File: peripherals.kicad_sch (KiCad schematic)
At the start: 14 parts, among them U5 FT230XQ

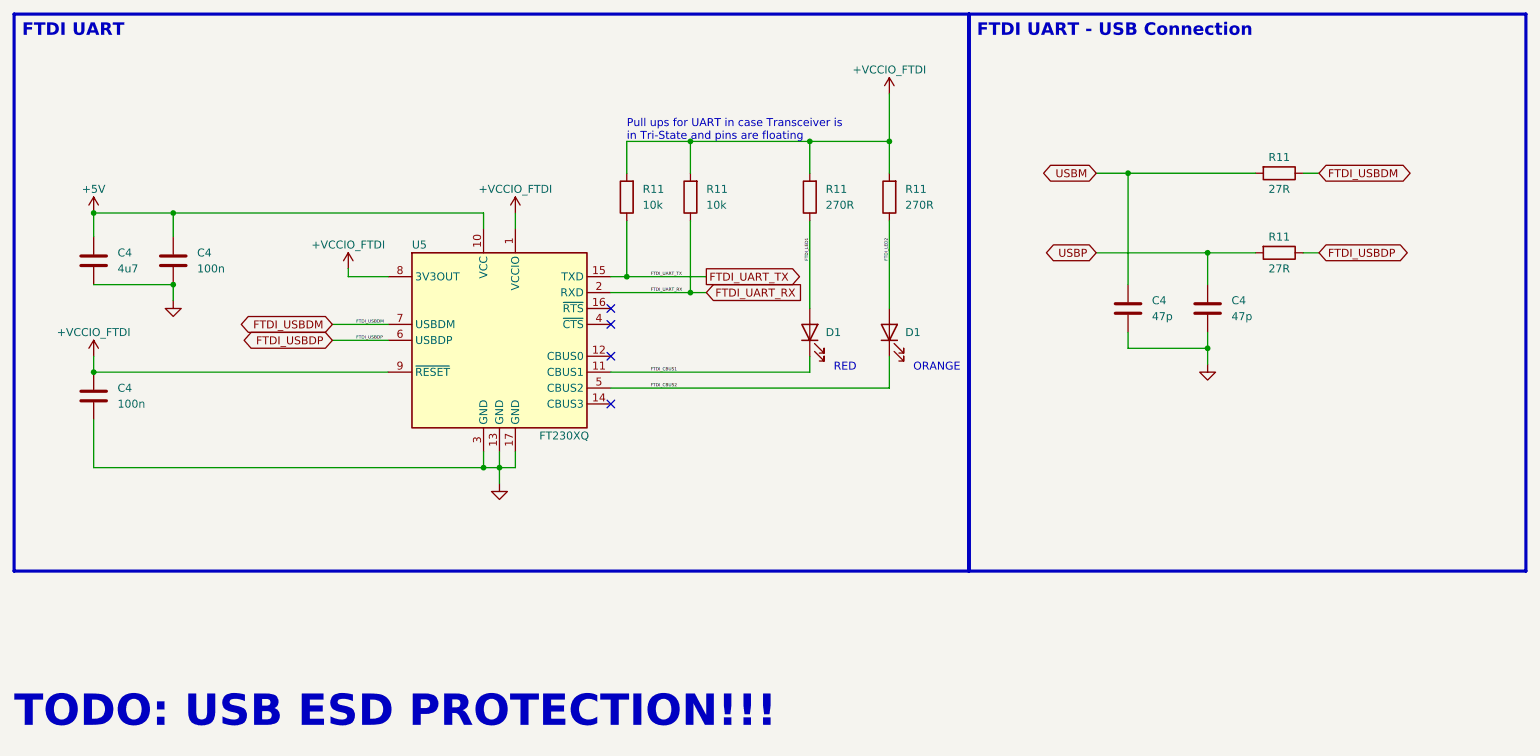
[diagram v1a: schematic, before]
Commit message: Schematic is done for now, starting layout
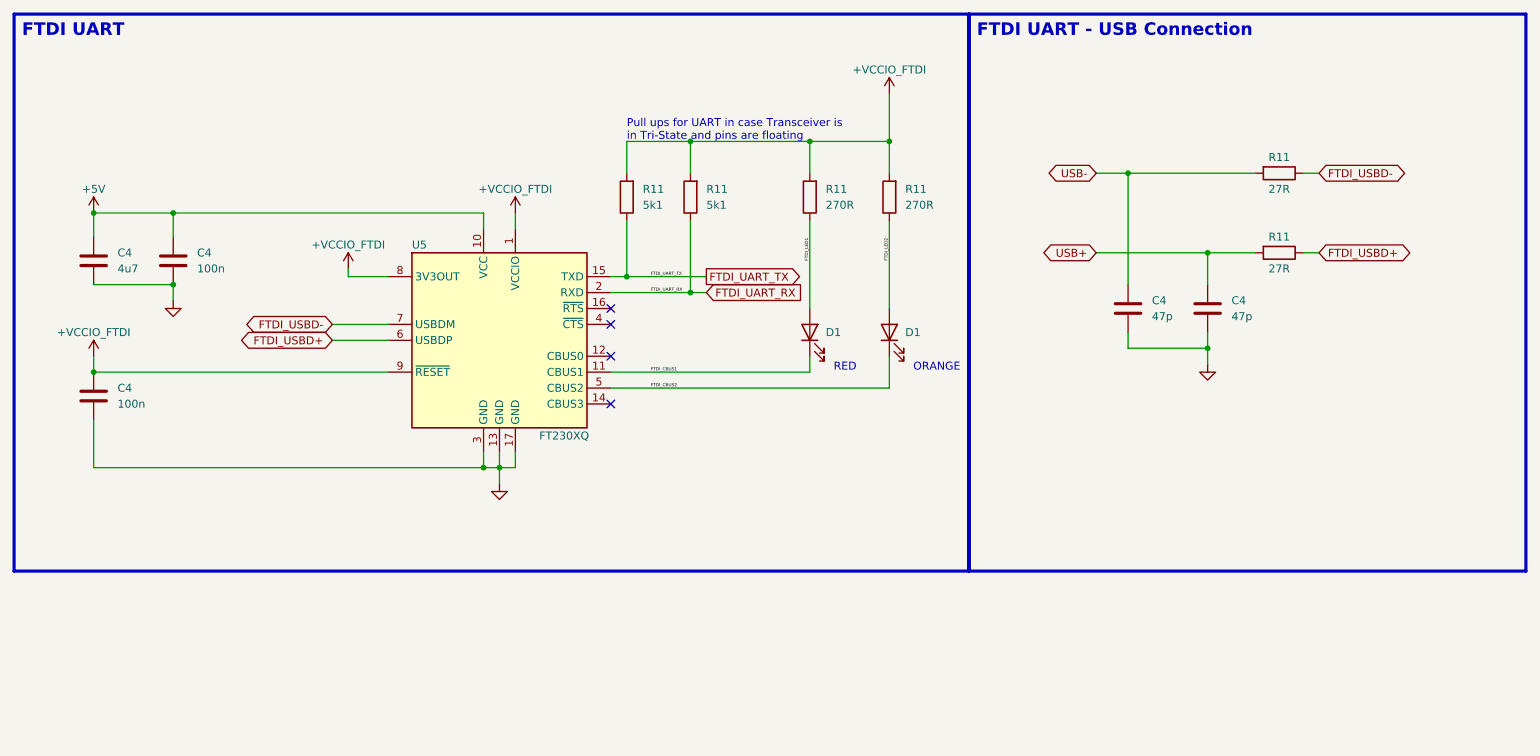
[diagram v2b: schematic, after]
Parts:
- D1: Distributor Link (none) -> https://www.mouser.de/ProductDetail/Lumex/SML-LX0402SIC-TR?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; MFN SML-LX0402SIC-TR -> (none); Manufacturer (none) -> Lumex; Manufacturer Number (none) -> SML-LX0402SIC-TR
- D1: Distributor Link (none) -> https://www.mouser.de/ProductDetail/Lumex/SML-LX0402SOC-TR?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; MFN SML-LX0402SOC-TR -> (none); Manufacturer (none) -> Lumex; Manufacturer Number (none) -> SML-LX0402SOC-TR
- R11: value 10k -> 5k1
- U5: Distributor Link (none) -> https://www.mouser.de/ProductDetail/FTDI/FT230XQ-R?qs=Gp1Yz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; Manufacturer (none) -> FTDI; Manufacturer Number (none) -> FT230XQ-R
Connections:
- net FTDI_USBDM renamed FTDI_USBD-
- net FTDI_USBDP renamed FTDI_USBD+
- net USBM renamed USB-
- net USBP renamed USB+
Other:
- note removed: "TODO: USB ESD PROTECTION!!!"
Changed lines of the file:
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@@
     (effects (font (size 2 2) (thickness 0.254) bold (color 100 100 100 1)) (justify left bottom))
-  )
-  (text "TODO: USB ESD PROTECTION!!!" (at 25.4 139.7 0)
-    (effects (font (size 5 5) (thickness 1) bold (color 150 0 0 1)) (justify left bottom))
   )
   (text "Pull ups for UART in case Transceiver is\nin Tri-State and pins are floating"
@@
     )
   )
-  (label "FTDI_USBDP" (at 80.01 77.47 0) (fields_autoplaced)
-    (effects (font (size 0.5 0.5)) (justify left bottom))
-    (property "Netclass" "UART" (at 80.01 77.97 0)
-      (effects (font (size 0.5 0.5) italic) (justify left))
-    )
-  )
   (label "FTDI_LED1" (at 152.4 64.77 90) (fields_autoplaced)
     (effects (font (size 0.5 0.5)) (justify left bottom))
@@
     )
   )
-  (label "FTDI_USBDM" (at 80.01 74.93 0) (fields_autoplaced)
-    (effects (font (size 0.5 0.5)) (justify left bottom))
-    (property "Netclass" "UART" (at 80.01 75.43 0)
-      (effects (font (size 0.5 0.5) italic) (justify left))
-    )
-  )
   (label "FTDI_LED2" (at 165.1 64.77 90) (fields_autoplaced)
     (effects (font (size 0.5 0.5)) (justify left bottom))
@@
     )
   )
-  (global_label "FTDI_USBDP" (shape bidirectional) (at 76.2 77.47 180) (fields_autoplaced)
+  (global_label "FTDI_USBD+" (shape bidirectional) (at 76.2 77.47 180) (fields_autoplaced)
     (effects (font (size 1.27 1.27)) (justify right))
-    (property "Intersheetrefs" "${INTERSHEET_REFS}" (at 60.8549 77.47 0)
+    (property "Intersheetrefs" "${INTERSHEET_REFS}" (at 60.5525 77.47 0)
       (effects (font (size 1.27 1.27)) (justify right) hide)
     )
   )
-  (global_label "USBP" (shape bidirectional) (at 198.12 63.5 180) (fields_autoplaced)
+  (global_label "USB+" (shape bidirectional) (at 198.12 63.5 180) (fields_autoplaced)
     (effects (font (size 1.27 1.27)) (justify right))
-    (property "Intersheetrefs" "${INTERSHEET_REFS}" (at 188.9435 63.5 0)
+    (property "Intersheetrefs" "${INTERSHEET_REFS}" (at 188.6411 63.5 0)
       (effects (font (size 1.27 1.27)) (justify right) hide)
     )
   )
-  (global_label "FTDI_USBDM" (shape bidirectional) (at 76.2 74.93 180) (fields_autoplaced)
+  (global_label "FTDI_USBD-" (shape bidirectional) (at 76.2 74.93 180) (fields_autoplaced)
     (effects (font (size 1.27 1.27)) (justify right))
-    (property "Intersheetrefs" "${INTERSHEET_REFS}" (at 60.6735 74.93 0)
+    (property "Intersheetrefs" "${INTERSHEET_REFS}" (at 60.5525 74.93 0)
       (effects (font (size 1.27 1.27)) (justify right) hide)
     )
   )
-  (global_label "FTDI_USBDM" (shape bidirectional) (at 233.68 50.8 0) (fields_autoplaced)
+  (global_label "FTDI_USBD-" (shape bidirectional) (at 233.68 50.8 0) (fields_autoplaced)
     (effects (font (size 1.27 1.27)) (justify left))
-    (property "Intersheetrefs" "${INTERSHEET_REFS}" (at 249.2065 50.8 0)
+    (property "Intersheetrefs" "${INTERSHEET_REFS}" (at 249.3275 50.8 0)
       (effects (font (size 1.27 1.27)) (justify left) hide)
     )
@@
     )
   )
-  (global_label "FTDI_USBDP" (shape bidirectional) (at 233.68 63.5 0) (fields_autoplaced)
+  (global_label "FTDI_USBD+" (shape bidirectional) (at 233.68 63.5 0) (fields_autoplaced)
     (effects (font (size 1.27 1.27)) (justify left))
-    (property "Intersheetrefs" "${INTERSHEET_REFS}" (at 249.0251 63.5 0)
+    (property "Intersheetrefs" "${INTERSHEET_REFS}" (at 249.3275 63.5 0)
       (effects (font (size 1.27 1.27)) (justify left) hide)
     )
@@
     )
   )
-  (global_label "USBM" (shape bidirectional) (at 198.12 50.8 180) (fields_autoplaced)
+  (global_label "USB-" (shape bidirectional) (at 198.12 50.8 180) (fields_autoplaced)
     (effects (font (size 1.27 1.27)) (justify right))
-    (property "Intersheetrefs" "${INTERSHEET_REFS}" (at 188.7621 50.8 0)
+    (property "Intersheetrefs" "${INTERSHEET_REFS}" (at 188.6411 50.8 0)
       (effects (font (size 1.27 1.27)) (justify right) hide)
     )
@@
     )
     (property "Datasheet" "https://www.ftdichip.com/Support/Documents/DataSheets/ICs/DS_FT230X.pdf" (at 102.87 77.47 0)
+      (effects (font (size 1.27 1.27)) hide)
+    )
+    (property "Distributor Link" "https://www.mouser.de/ProductDetail/FTDI/FT230XQ-R?qs=Gp1Yz1mis3VvmXwyDmIHOg%3D%3D" (at 102.87 77.47 0)
+      (effects (font (size 1.27 1.27)) hide)
+    )
+    (property "Manufacturer" "FTDI" (at 102.87 77.47 0)
+      (effects (font (size 1.27 1.27)) hide)
+    )
+    (property "Manufacturer Number" "FT230XQ-R" (at 102.87 77.47 0)
       (effects (font (size 1.27 1.27)) hide)
     )
@@
       (effects (font (size 1.27 1.27)) hide)
     )
+    (property "Distributor Link" "" (at 38.1 86.36 0)
+      (effects (font (size 1.27 1.27)) hide)
+    )
+    (property "Manufacturer" "" (at 38.1 86.36 0)
+      (effects (font (size 1.27 1.27)) hide)
+    )
     (pin "1")
     (pin "2")
@@
       (effects (font (size 1.27 1.27)) hide)
     )
+    (property "Distributor Link" "" (at 227.33 50.8 0)
+      (effects (font (size 1.27 1.27)) hide)
+    )
+    (property "Manufacturer" "" (at 227.33 50.8 0)
+      (effects (font (size 1.27 1.27)) hide)
+    )
     (pin "1")
     (pin "2")
@@
       (effects (font (size 1.27 1.27)) hide)
     )
+    (property "Distributor Link" "" (at 165.1 54.61 0)
+      (effects (font (size 1.27 1.27)) hide)
+    )
+    (property "Manufacturer" "" (at 165.1 54.61 0)
+      (effects (font (size 1.27 1.27)) hide)
+    )
     (pin "1")
     (pin "2")
@@
       (effects (font (size 1.27 1.27)) (justify right))
     )
-    (property "Value" "10k" (at 125.73 55.88 0)
+    (property "Value" "5k1" (at 125.73 55.88 0)
       (effects (font (size 1.27 1.27)) (justify right))
     )
@@
       (effects (font (size 1.27 1.27)) hide)
     )
+    (property "Distributor Link" "" (at 123.19 54.61 0)
+      (effects (font (size 1.27 1.27)) hide)
+    )
+    (property "Manufacturer" "" (at 123.19 54.61 0)
+      (effects (font (size 1.27 1.27)) hide)
+    )
     (pin "1")
     (pin "2")
@@
       (effects (font (size 1.27 1.27)) hide)
     )
+    (property "Distributor Link" "" (at 203.2 72.39 0)
+      (effects (font (size 1.27 1.27)) hide)
+    )
+    (property "Manufacturer" "" (at 203.2 72.39 0)
+      (effects (font (size 1.27 1.27)) hide)
+    )
     (pin "1")
     (pin "2")
@@
     )
     (property "Datasheet" "~" (at 227.33 63.5 0)
+      (effects (font (size 1.27 1.27)) hide)
+    )
+    (property "Distributor Link" "" (at 227.33 63.5 0)
+      (effects (font (size 1.27 1.27)) hide)
+    )
+    (property "Manufacturer" "" (at 227.33 63.5 0)
       (effects (font (size 1.27 1.27)) hide)
     )
@@
       (effects (font (size 1.27 1.27)) hide)
     )
-    (property "MFN" "SML-LX0402SIC-TR" (at 152.4 76.2 90)
+    (property "Manufacturer Number" "SML-LX0402SIC-TR" (at 152.4 76.2 90)
+      (effects (font (size 1.27 1.27)) hide)
+    )
+    (property "Distributor Link" "https://www.mouser.de/ProductDetail/Lumex/SML-LX0402SIC-TR?qs=CpNDN%2FcFIdfSV9iBmfgYzQ%3D%3D" (at 152.4 76.2 0)
+      (effects (font (size 1.27 1.27)) hide)
+    )
+    (property "Manufacturer" "Lumex" (at 152.4 76.2 0)
       (effects (font (size 1.27 1.27)) hide)
     )
@@
       (effects (font (size 1.27 1.27)) hide)
     )
+    (property "Distributor Link" "" (at 215.9 72.39 0)
+      (effects (font (size 1.27 1.27)) hide)
+    )
+    (property "Manufacturer" "" (at 215.9 72.39 0)
+      (effects (font (size 1.27 1.27)) hide)
+    )
     (pin "1")
     (pin "2")
@@
       (effects (font (size 1.27 1.27)) hide)
     )
+    (property "Distributor Link" "" (at 38.1 64.77 0)
+      (effects (font (size 1.27 1.27)) hide)
+    )
+    (property "Manufacturer" "" (at 38.1 64.77 0)
+      (effects (font (size 1.27 1.27)) hide)
+    )
     (pin "1")
     (pin "2")
@@
     )
     (property "Datasheet" "~" (at 152.4 54.61 0)
+      (effects (font (size 1.27 1.27)) hide)
+    )
+    (property "Distributor Link" "" (at 152.4 54.61 0)
+      (effects (font (size 1.27 1.27)) hide)
+    )
+    (property "Manufacturer" "" (at 152.4 54.61 0)
       (effects (font (size 1.27 1.27)) hide)
     )
@@
       (effects (font (size 1.27 1.27)) (justify right))
     )
-    (property "Value" "10k" (at 135.89 55.88 0)
+    (property "Value" "5k1" (at 135.89 55.88 0)
       (effects (font (size 1.27 1.27)) (justify right))
     )
@@
     )
     (property "Datasheet" "~" (at 133.35 54.61 0)
+      (effects (font (size 1.27 1.27)) hide)
+    )
+    (property "Distributor Link" "" (at 133.35 54.61 0)
+      (effects (font (size 1.27 1.27)) hide)
+    )
+    (property "Manufacturer" "" (at 133.35 54.61 0)
       (effects (font (size 1.27 1.27)) hide)
     )
@@
       (effects (font (size 1.27 1.27)) hide)
     )
-    (property "MFN" "SML-LX0402SOC-TR" (at 165.1 76.2 90)
+    (property "Manufacturer Number" "SML-LX0402SOC-TR" (at 165.1 76.2 90)
+      (effects (font (size 1.27 1.27)) hide)
+    )
+    (property "Distributor Link" "https://www.mouser.de/ProductDetail/Lumex/SML-LX0402SOC-TR?qs=jCymNF74TgXR3H6Hl8gtyA%3D%3D" (at 165.1 76.2 0)
+      (effects (font (size 1.27 1.27)) hide)
+    )
+    (property "Manufacturer" "Lumex" (at 165.1 76.2 0)
       (effects (font (size 1.27 1.27)) hide)
     )
@@
       (effects (font (size 1.27 1.27)) hide)
     )
+    (property "Distributor Link" "" (at 50.8 64.77 0)
+      (effects (font (size 1.27 1.27)) hide)
+    )
+    (property "Manufacturer" "" (at 50.8 64.77 0)
+      (effects (font (size 1.27 1.27)) hide)
+    )

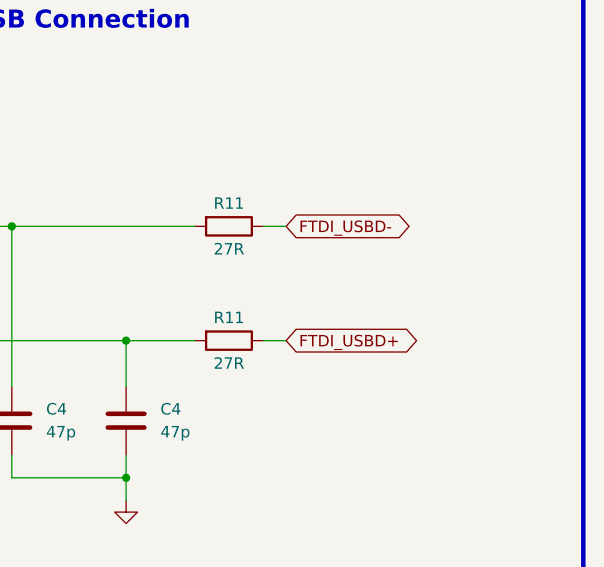
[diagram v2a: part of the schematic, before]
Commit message: Layout and routing basically done, check again before delivering
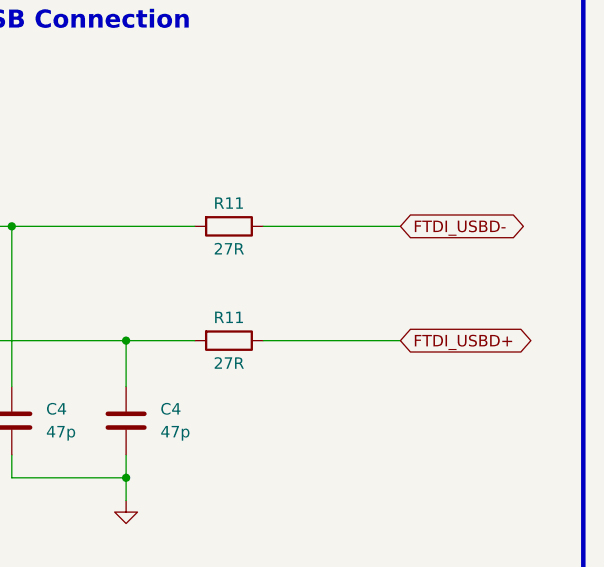
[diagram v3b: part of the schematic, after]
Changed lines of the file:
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@@
-    (stroke (width 0) (type default))
-  )
-  (wire (pts (xy 231.14 63.5) (xy 233.68 63.5))
     (stroke (width 0) (type default))
   )
@@
     (stroke (width 0) (type default))
   )
+  (wire (pts (xy 231.14 63.5) (xy 246.38 63.5))
+    (stroke (width 0) (type default))
+  )
   (wire (pts (xy 100.33 57.15) (xy 100.33 59.69))
     (stroke (width 0) (type default))
@@
     (stroke (width 0) (type default))
   )
-  (wire (pts (xy 231.14 50.8) (xy 233.68 50.8))
+  (wire (pts (xy 231.14 50.8) (xy 246.38 50.8))
     (stroke (width 0) (type default))
   )
@@
     )
   )
-  (global_label "FTDI_USBD-" (shape bidirectional) (at 233.68 50.8 0) (fields_autoplaced)
+  (global_label "FTDI_USBD-" (shape bidirectional) (at 246.38 50.8 0) (fields_autoplaced)
     (effects (font (size 1.27 1.27)) (justify left))
-    (property "Intersheetrefs" "${INTERSHEET_REFS}" (at 249.3275 50.8 0)
+    (property "Intersheetrefs" "${INTERSHEET_REFS}" (at 262.0275 50.8 0)
       (effects (font (size 1.27 1.27)) (justify left) hide)
     )
@@
     )
   )
-  (global_label "FTDI_USBD+" (shape bidirectional) (at 233.68 63.5 0) (fields_autoplaced)
+  (global_label "FTDI_USBD+" (shape bidirectional) (at 246.38 63.5 0) (fields_autoplaced)
     (effects (font (size 1.27 1.27)) (justify left))
-    (property "Intersheetrefs" "${INTERSHEET_REFS}" (at 249.3275 63.5 0)
+    (property "Intersheetrefs" "${INTERSHEET_REFS}" (at 262.0275 63.5 0)
       (effects (font (size 1.27 1.27)) (justify left) hide)
     )
